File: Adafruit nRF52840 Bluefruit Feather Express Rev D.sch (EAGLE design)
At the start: 42 parts, among them IC2 GD25Q16, Q3 DMG2305, SW1 KMR2, SW2 KMR2, U2 AP2112(3.3V), U3 MCP73831T-2ACI/OT, X1 4u20329, X2 2x5 0.05", X3 JSTPH, Y2 32.768

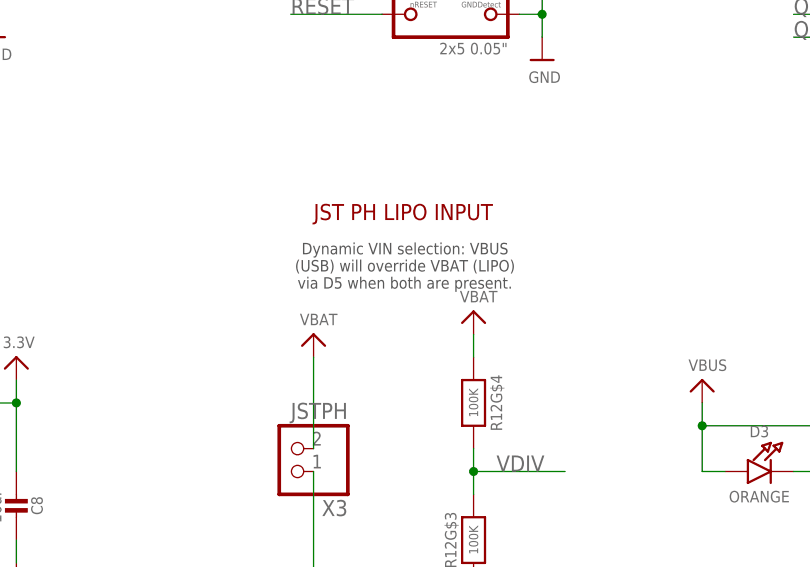
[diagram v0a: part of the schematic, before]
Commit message: Fixing typo: D5 -> D1
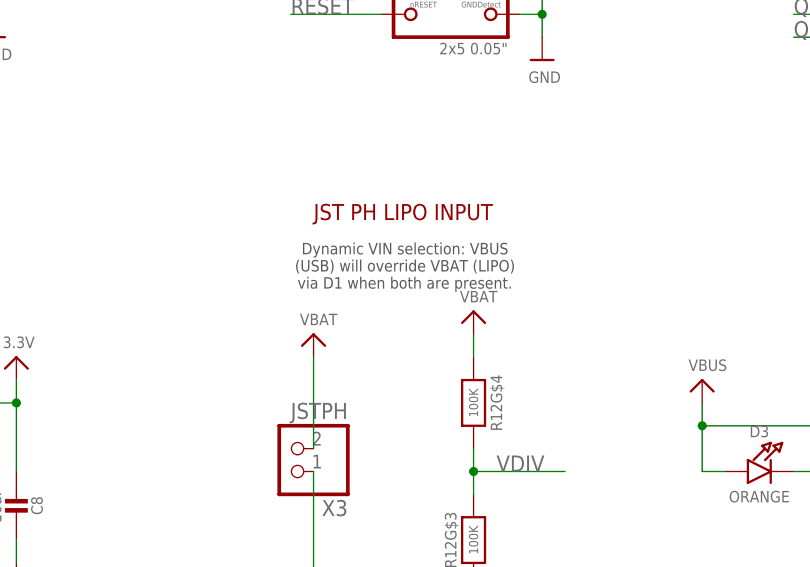
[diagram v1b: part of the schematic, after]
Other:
- note added: "Dynamic VIN selection: VBUS (USB) will override VBAT (LIPO) via D1 when both are present."
- note removed: "Dynamic VIN selection: VBUS (USB) will override VBAT (LIPO) via D5 when both are present."
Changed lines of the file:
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@@
 <text x="170.18" y="55.88" size="1.27" layer="97" align="center">Dynamic VIN selection: VBUS
 (USB) will override VBAT (LIPO)
-via D5 when both are present.</text>
+via D1 when both are present.</text>
 <text x="96.52" y="45.72" size="1.778" layer="97">Dropout Voltage (25°C):
 100mA: ~250/~40mV
